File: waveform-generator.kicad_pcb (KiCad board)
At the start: 2 copper layers, 50.8 x 50.8 mm, 57 parts, among them J1 USB_B, J2 EXT_CLK, J3 VOUT, J4 CONN_02X09, U1 LD1117S33TR, U2 93LC46BT, U3 AD9837, U4 FT2232H, Y1 12MHz, Y2 OXETGCJANF

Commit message: Replace slots with holes.
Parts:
- J1: footprint Connectors:USB_Micro-B -> USB_Micro-B-circular
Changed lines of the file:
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@@
-(kicad_pcb (version 4) (host pcbnew 4.0.6)
+(kicad_pcb (version 4) (host pcbnew 4.0.6-e0-6349~53~ubuntu16.04.1)
   (general
     (links 146)
@@
     (uvia_drill 0.1)
   )
+  (module USB_Micro-B-circular locked (layer F.Cu)
+    (at 48.26 21.59 180)
+    (descr "Micro USB Type B Receptacle")
+    (tags "USB USB_B USB_micro USB_OTG")
+    (attr smd)
+    (fp_text reference J1 (at 0 -3.24 180) (layer F.SilkS)
+      (effects (font (size 1 1) (thickness 0.15)))
+    )
+    (fp_text value USB_B (at 0 5.01 180) (layer F.Fab)
+      (effects (font (size 1 1) (thickness 0.15)))
+    )
+    (fp_line (start -4.6 -2.59) (end 4.6 -2.59) (layer F.CrtYd) (width 0.05))
+    (fp_line (start 4.6 -2.59) (end 4.6 4.26) (layer F.CrtYd) (width 0.05))
+    (fp_line (start 4.6 4.26) (end -4.6 4.26) (layer F.CrtYd) (width 0.05))
+    (fp_line (start -4.6 4.26) (end -4.6 -2.59) (layer F.CrtYd) (width 0.05))
+    (fp_line (start -4.35 4.03) (end 4.35 4.03) (layer F.SilkS) (width 0.12))
+    (fp_line (start -4.35 -2.38) (end 4.35 -2.38) (layer F.SilkS) (width 0.12))
+    (fp_line (start 4.35 -2.38) (end 4.35 4.03) (layer F.SilkS) (width 0.12))
+    (fp_line (start 4.35 2.8) (end -4.35 2.8) (layer F.SilkS) (width 0.12))
+    (fp_line (start -4.35 4.03) (end -4.35 -2.38) (layer F.SilkS) (width 0.12))
+    (pad 1 smd rect (at -1.3 -1.35 270) (size 1.35 0.4) (layers F.Cu F.Paste F.Mask)
+      (net 1 "Net-(C3-Pad1)"))
+    (pad 2 smd rect (at -0.65 -1.35 270) (size 1.35 0.4) (layers F.Cu F.Paste F.Mask)
+      (net 15 USB_D-))
+    (pad 3 smd rect (at 0 -1.35 270) (size 1.35 0.4) (layers F.Cu F.Paste F.Mask)
+      (net 16 USB_D+))
+    (pad 4 smd rect (at 0.65 -1.35 270) (size 1.35 0.4) (layers F.Cu F.Paste F.Mask)
+      (net 2 GNDA))
+    (pad 5 smd rect (at 1.3 -1.35 270) (size 1.35 0.4) (layers F.Cu F.Paste F.Mask)
+      (net 2 GNDA))
+    (pad 6 thru_hole circle (at -2.5 -1.35 270) (size 1.25 1.25) (drill 0.85) (layers *.Cu *.Mask))
+    (pad 6 thru_hole circle (at 2.5 -1.35 270) (size 1.25 1.25) (drill 0.85) (layers *.Cu *.Mask))
+    (pad 6 thru_hole circle (at -3.5 1.35 270) (size 1.55 1.55) (drill 1.15) (layers *.Cu *.Mask))
+    (pad 6 thru_hole circle (at 3.5 1.35 270) (size 1.55 1.55) (drill 1.15) (layers *.Cu *.Mask))
+  )
   (module Mounting_Holes:MountingHole_3.5mm (layer F.Cu)
     (at 69.85 64.77)
@@
       (rotate (xyz 0 0 180))
     )
-  )
-  (module Connectors:USB_Micro-B locked (layer F.Cu)
-    (at 48.26 21.59 180)
-    (descr "Micro USB Type B Receptacle")
-    (tags "USB USB_B USB_micro USB_OTG")
-    (attr smd)
-    (fp_text reference J1 (at 0 -3.24 180) (layer F.SilkS)
-      (effects (font (size 1 1) (thickness 0.15)))
-    )
-    (fp_text value USB_B (at 0 5.01 180) (layer F.Fab)
-      (effects (font (size 1 1) (thickness 0.15)))
-    )
-    (fp_line (start -4.6 -2.59) (end 4.6 -2.59) (layer F.CrtYd) (width 0.05))
-    (fp_line (start 4.6 -2.59) (end 4.6 4.26) (layer F.CrtYd) (width 0.05))
-    (fp_line (start 4.6 4.26) (end -4.6 4.26) (layer F.CrtYd) (width 0.05))
-    (fp_line (start -4.6 4.26) (end -4.6 -2.59) (layer F.CrtYd) (width 0.05))
-    (fp_line (start -4.35 4.03) (end 4.35 4.03) (layer F.SilkS) (width 0.12))
-    (fp_line (start -4.35 -2.38) (end 4.35 -2.38) (layer F.SilkS) (width 0.12))
-    (fp_line (start 4.35 -2.38) (end 4.35 4.03) (layer F.SilkS) (width 0.12))
-    (fp_line (start 4.35 2.8) (end -4.35 2.8) (layer F.SilkS) (width 0.12))
-    (fp_line (start -4.35 4.03) (end -4.35 -2.38) (layer F.SilkS) (width 0.12))
-    (pad 1 smd rect (at -1.3 -1.35 270) (size 1.35 0.4) (layers F.Cu F.Paste F.Mask)
-      (net 1 "Net-(C3-Pad1)"))
-    (pad 2 smd rect (at -0.65 -1.35 270) (size 1.35 0.4) (layers F.Cu F.Paste F.Mask)
-      (net 15 USB_D-))
-    (pad 3 smd rect (at 0 -1.35 270) (size 1.35 0.4) (layers F.Cu F.Paste F.Mask)
-      (net 16 USB_D+))
-    (pad 4 smd rect (at 0.65 -1.35 270) (size 1.35 0.4) (layers F.Cu F.Paste F.Mask)
-      (net 2 GNDA))
-    (pad 5 smd rect (at 1.3 -1.35 270) (size 1.35 0.4) (layers F.Cu F.Paste F.Mask)
-      (net 2 GNDA))
-    (pad 6 thru_hole oval (at -2.5 -1.35 270) (size 0.95 1.25) (drill oval 0.55 0.85) (layers *.Cu *.Mask))
-    (pad 6 thru_hole oval (at 2.5 -1.35 270) (size 0.95 1.25) (drill oval 0.55 0.85) (layers *.Cu *.Mask))
-    (pad 6 thru_hole oval (at -3.5 1.35 270) (size 1.55 1) (drill oval 1.15 0.5) (layers *.Cu *.Mask))
-    (pad 6 thru_hole oval (at 3.5 1.35 270) (size 1.55 1) (drill oval 1.15 0.5) (layers *.Cu *.Mask))
   )
   (module Connectors:SMA_THT_Jack_Straight locked (layer F.Cu)
@@
   (segment (start 33.3575 20.193) (end 33.3575 21.454) (width 0.381) (layer F.Cu) (net 1) (status 10))
   (segment (start 33.3575 21.454) (end 32.4345 22.377) (width 0.381) (layer F.Cu) (net 1) (status 20))
+  (segment (start 46.99 21.845) (end 46.99 21.59) (width 0.381) (layer F.Cu) (net 2))
+  (segment (start 47.61 22.465) (end 46.99 21.845) (width 0.381) (layer F.Cu) (net 2))
+  (segment (start 47.61 22.94) (end 47.61 22.465) (width 0.381) (layer F.Cu) (net 2))
+  (segment (start 46.96 21.62) (end 46.99 21.59) (width 0.381) (layer F.Cu) (net 2))
+  (segment (start 46.96 22.94) (end 46.96 21.62) (width 0.381) (layer F.Cu) (net 2))
+  (via (at 46.99 21.59) (size 0.5588) (drill 0.254) (layers F.Cu B.Cu) (net 2))
   (segment (start 50.72117 62.382711) (end 50.72117 61.98758) (width 0.254) (layer F.Cu) (net 2))
   (segment (start 49.76 63) (end 50.514 63) (width 0.254) (layer F.Cu) (net 2))
@@
   (segment (start 47.61 23.7005) (end 47.3075 24.003) (width 0.381) (layer F.Cu) (net 2))
   (via (at 47.3075 24.003) (size 0.5588) (drill 0.254) (layers F.Cu B.Cu) (net 2))
-  (segment (start 46.96 22.94) (end 46.96 22.128) (width 0.381) (layer F.Cu) (net 2) (status 10))
-  (segment (start 46.96 22.128) (end 47.3075 21.7805) (width 0.381) (layer F.Cu) (net 2))
-  (segment (start 47.61 22.94) (end 47.61 22.083) (width 0.381) (layer F.Cu) (net 2) (status 10))
-  (segment (start 47.61 22.083) (end 47.3075 21.7805) (width 0.381) (layer F.Cu) (net 2))
-  (via (at 47.3075 21.7805) (size 0.5588) (drill 0.254) (layers F.Cu B.Cu) (net 2))
   (segment (start 37.0345 22.377) (end 37.0345 20.7785) (width 0.381) (layer F.Cu) (net 2) (status 10))
   (segment (start 37.0345 20.7785) (end 37.0205 20.7645) (width 0.381) (layer F.Cu) (net 2))
@@
   (via (at 45.0215 47.3075) (size 0.5588) (drill 0.254) (layers F.Cu B.Cu) (net 2))
   (segment (start 25.4 33.401) (end 25.4 34.29) (width 0.635) (layer F.Cu) (net 2) (status 30))
+  (segment (start 45.099131 21.717) (end 44.704 21.717) (width 0.635) (layer B.Cu) (net 3))
+  (segment (start 61.0235 18.7325) (end 48.083631 18.7325) (width 0.635) (layer B.Cu) (net 3))
+  (segment (start 61.595 19.304) (end 61.0235 18.7325) (width 0.635) (layer B.Cu) (net 3))
+  (segment (start 48.083631 18.7325) (end 45.099131 21.717) (width 0.635) (layer B.Cu) (net 3))
   (segment (start 34.9885 23.8125) (end 35.941 24.765) (width 0.635) (layer F.Cu) (net 3))
   (segment (start 35.941 24.765) (end 37.592 24.765) (width 0.635) (layer F.Cu) (net 3))
@@
   (segment (start 44.703992 21.717008) (end 44.704 21.717) (width 0.635) (layer B.Cu) (net 3))
   (segment (start 43.942 21.717008) (end 44.703992 21.717008) (width 0.635) (layer B.Cu) (net 3))
-  (segment (start 46.262034 21.717) (end 45.099131 21.717) (width 0.635) (layer B.Cu) (net 3))
-  (segment (start 49.246534 18.7325) (end 46.262034 21.717) (width 0.635) (layer B.Cu) (net 3))
-  (segment (start 61.0235 18.7325) (end 49.246534 18.7325) (width 0.635) (layer B.Cu) (net 3))
-  (segment (start 45.099131 21.717) (end 44.704 21.717) (width 0.635) (layer B.Cu) (net 3))
-  (segment (start 61.595 19.304) (end 61.0235 18.7325) (width 0.635) (layer B.Cu) (net 3))
   (via (at 44.704 21.717) (size 0.5588) (drill 0.254) (layers F.Cu B.Cu) (net 3))
   (via (at 43.942 21.717008) (size 0.5588) (drill 0.254) (layers F.Cu B.Cu) (net 3))

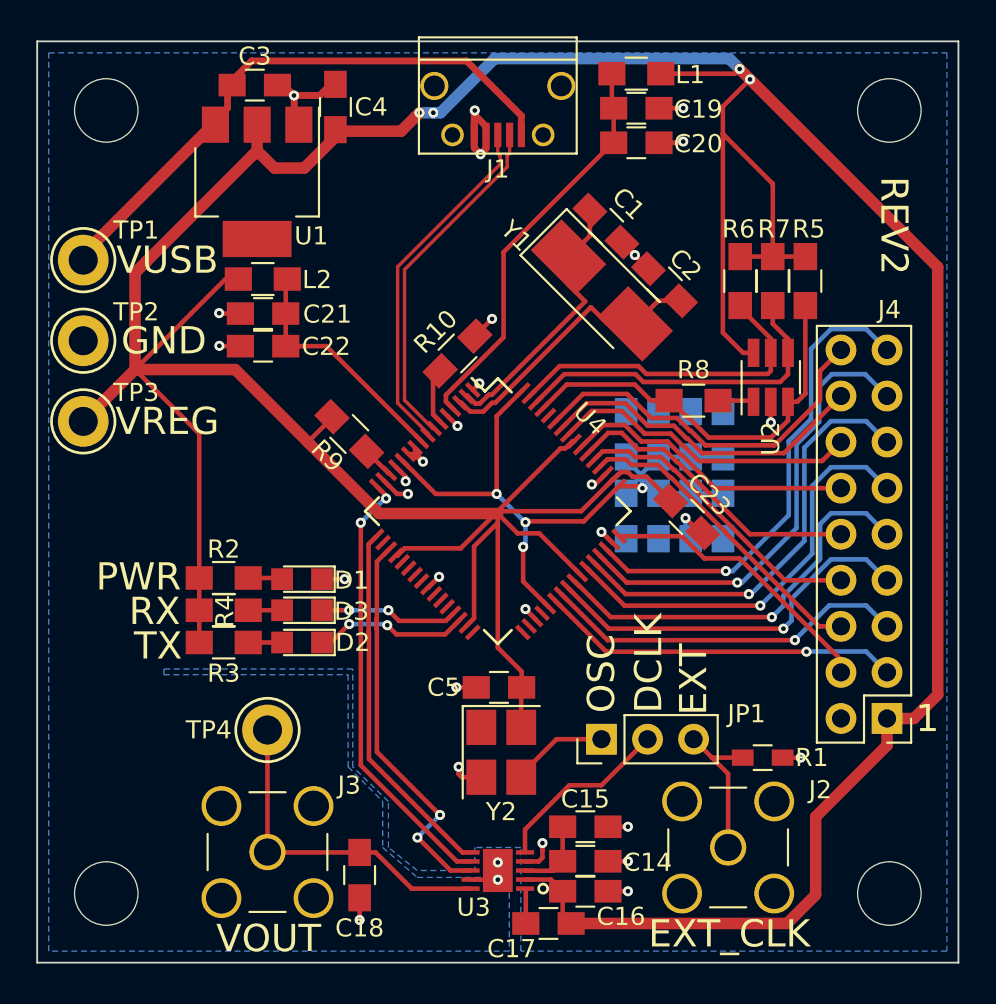
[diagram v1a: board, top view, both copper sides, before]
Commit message: Fixup analog-digital ground connection.
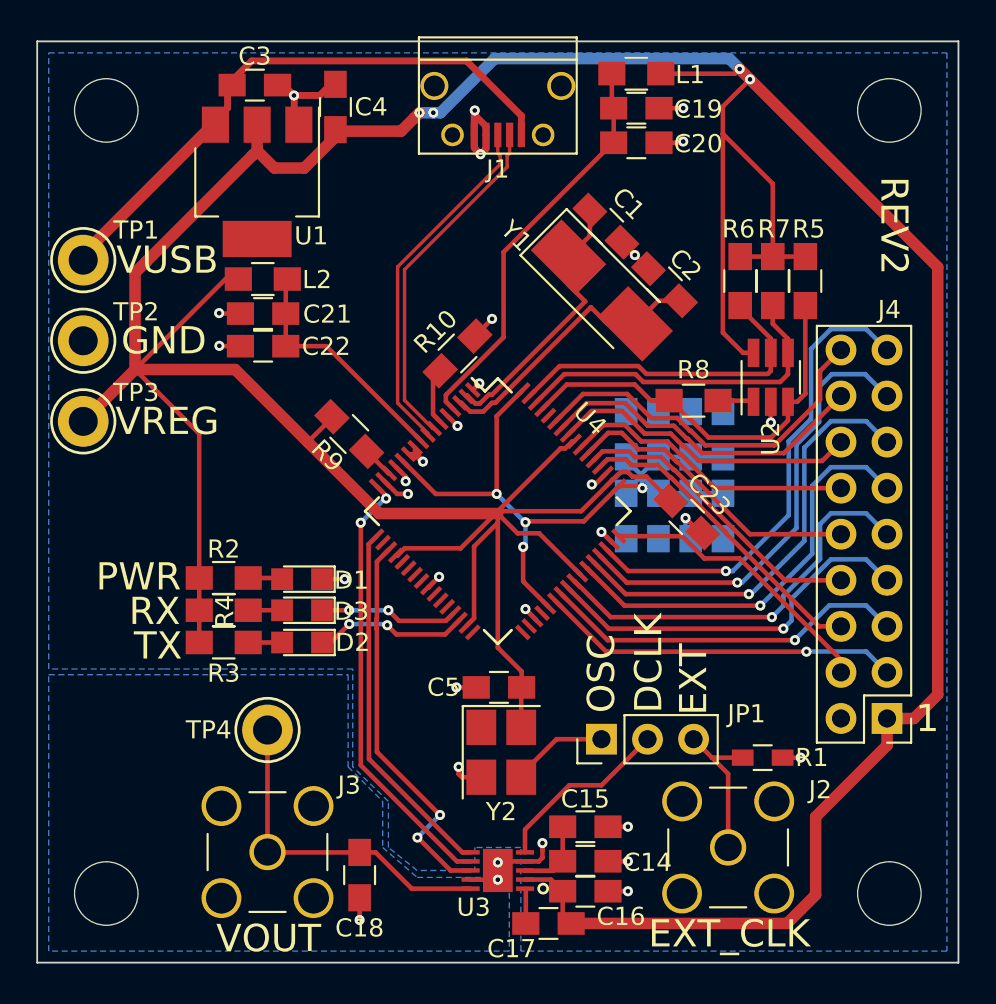
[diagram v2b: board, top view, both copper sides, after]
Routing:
- net GNDA: track 45.8 -> 47.5 mm
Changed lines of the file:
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@@
-(kicad_pcb (version 4) (host pcbnew 4.0.6-e0-6349~53~ubuntu16.04.1)
+(kicad_pcb (version 4) (host pcbnew 4.0.6)
   (general
     (links 146)
     (no_connects 0)
-    (area 22.809999 17.729999 73.710001 68.630001)
+    (area 18.563629 15.6272 86.895715 77.630001)
     (thickness 1.6)
     (drawings 27)
-    (tracks 544)
+    (tracks 546)
     (zones 0)
     (modules 57)
@@
     (aux_axis_origin 22.86 17.78)
     (grid_origin 22.86 17.78)
-    (visible_elements 7FFC4229)
+    (visible_elements 7FFC5229)
     (pcbplotparams
       (layerselection 0x010f0_80000001)
@@
   (segment (start 33.3575 20.193) (end 33.3575 21.454) (width 0.381) (layer F.Cu) (net 1) (status 10))
   (segment (start 33.3575 21.454) (end 32.4345 22.377) (width 0.381) (layer F.Cu) (net 1) (status 20))
+  (segment (start 49.76 63) (end 48.76 63) (width 0.254) (layer F.Cu) (net 2) (status C00000))
+  (segment (start 48.76 63) (end 48.26 63.5) (width 0.254) (layer F.Cu) (net 2) (status C00000))
   (segment (start 46.99 21.845) (end 46.99 21.59) (width 0.381) (layer F.Cu) (net 2))
   (segment (start 47.61 22.465) (end 46.99 21.845) (width 0.381) (layer F.Cu) (net 2))
@@
     (polygon
       (pts
-        (xy 73.025 67.945) (xy 49.53 67.945) (xy 49.53 62.23) (xy 46.99 62.23) (xy 46.99 63.5)
-        (xy 43.815 63.5) (xy 42.2275 62.23) (xy 42.2275 59.69) (xy 40.259 57.785) (xy 40.259 52.3875)
-        (xy 29.845 52.3875) (xy 29.845 52.705) (xy 40.005 52.705) (xy 40.005 57.785) (xy 41.91 59.69)
-        (xy 41.91 62.23) (xy 43.815 63.881) (xy 47.625 63.881) (xy 47.625 62.611) (xy 48.895 62.611)
-        (xy 48.895 67.945) (xy 23.495 67.945) (xy 23.495 18.415) (xy 73.025 18.415)
+        (xy 23.495 18.415) (xy 73.025 18.415) (xy 73.025 67.945) (xy 49.53 67.945) (xy 49.53 62.23)
+        (xy 46.99 62.23) (xy 46.99 63.5) (xy 43.815 63.5) (xy 42.2275 62.23) (xy 42.2275 59.69)
+        (xy 40.259 57.785) (xy 40.259 52.3875) (xy 29.845 52.3875) (xy 23.495 52.3875)
       )
     )
@@
       )
     )
+  )
+  (zone (net 2) (net_name GNDA) (layer B.Cu) (hatch edge 0.508)
+    (connect_pads (clearance 0.508))
+    (min_thickness 0.254)
+    (fill yes (arc_segments 16) (thermal_gap 0.508) (thermal_bridge_width 0.508))
+    (polygon
+      (pts
+        (xy 40.005 52.705) (xy 40.005 57.785) (xy 41.91 59.69) (xy 41.91 62.23) (xy 43.815 63.881)
+        (xy 47.625 63.881) (xy 47.625 62.611) (xy 48.895 62.611) (xy 48.895 67.945) (xy 23.495 67.945)
+        (xy 23.495 52.705) (xy 29.845 52.705)
+      )
+    )
